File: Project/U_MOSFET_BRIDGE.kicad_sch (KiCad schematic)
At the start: 14 parts, among them Q301 DMT68M8LFV-7, Q302 DMT68M8LFV-7

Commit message: More files cleanup
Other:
- company: Quasi Peak -> ${COMPANY}

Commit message: Cleanup ED A1 version
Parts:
- C303: symbol Device:CP -> Device:C_Polarized
- Q301, Q302: symbol eval_board_tmc6200-ta:DMT68M8LFV-7 -> QP_LIBRARY:DMT68M8LFV-7

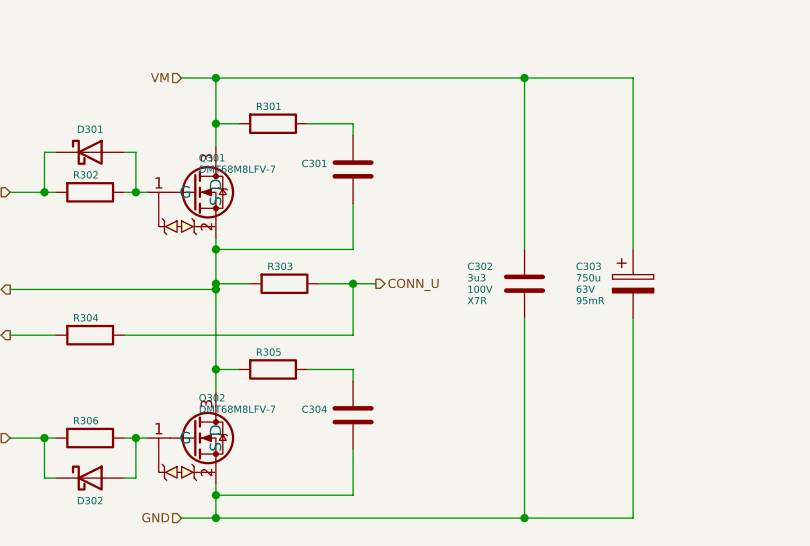
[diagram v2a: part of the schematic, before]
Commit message: Cleaning files, added testpoints
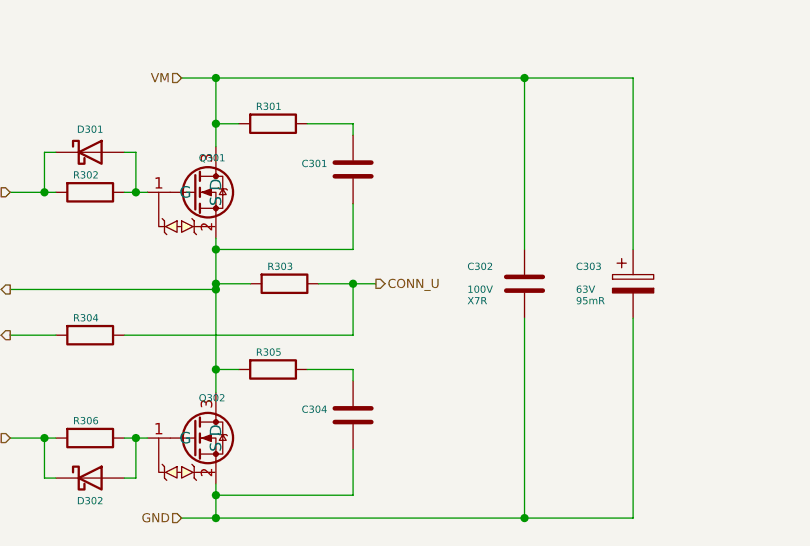
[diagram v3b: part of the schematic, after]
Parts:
- C301, C304: value C -> ~; footprint Capacitor_SMD:C_0402_1005Metric -> (none)
- C302: value 3u3 -> ~; footprint Capacitor_SMD:C_1812_4532Metric -> (none)
- C303: value 750u -> ~; footprint Capacitor_SMD:CP_Elec_18x17.5 -> (none)
- D301, D302: value D_Schottky -> ~; footprint Diode_SMD:D_SOD-123 -> (none)
- Q301, Q302: value DMT68M8LFV-7 -> ~; footprint eval_board_tmc6200-ta:DMT68M8LFV-7_PowerDI5060-8 -> (none)
- R301, R302, R304, R305, R306: value R -> ~; footprint Resistor_SMD:R_0402_1005Metric -> (none)
- R303: value R -> ~; footprint Resistor_SMD:R_1210_3225Metric -> (none)
